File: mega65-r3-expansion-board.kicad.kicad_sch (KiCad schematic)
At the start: 0 parts

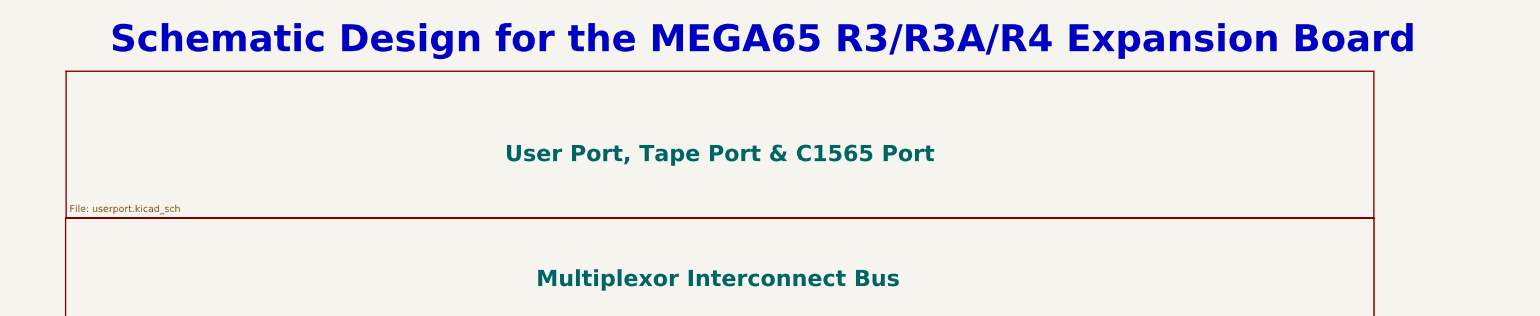
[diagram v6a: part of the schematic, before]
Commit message: begin peeling out C1565 port to separate sheet
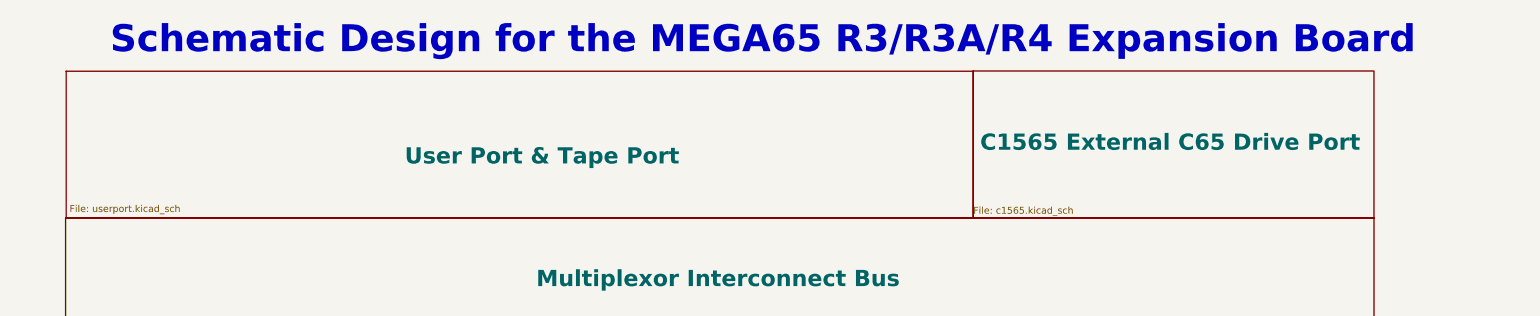
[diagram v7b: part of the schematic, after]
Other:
- sheet User Port, Tape Port & C1565 Port renamed User Port & Tape Port
- added sheet C1565 External C65 Drive Port (c1565.kicad_sch)
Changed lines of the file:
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@@
     (effects (font (size 5 5) (thickness 1) bold) (justify left bottom))
   )
-  (sheet (at 26.1366 63.8175) (size 242.443 27.2415)
+  (sheet (at 26.1366 63.8175) (size 168.1734 27.2415)
     (stroke (width 0.25) (type solid))
     (fill (color 54 142 255 1.0000))
-    (property "Sheetname" "User Port, Tape Port & C1565 Port" (at 107.4928 80.8482 0)
+    (property "Sheetname" "User Port & Tape Port" (at 88.9 81.28 0)
       (effects (font (size 3 3) bold) (justify left bottom))
     )
@@
       )
     )
+  )
+  (sheet (at 194.3072 63.7735) (size 74.2938 27.2606)
+    (stroke (width 0.25) (type solid))
+    (fill (color 0 0 255 1.0000))
+    (property "Sheetname" "C1565 External C65 Drive Port" (at 195.58 78.74 0)
+      (effects (font (size 3 3) bold) (justify left bottom))
+    )
+    (property "Sheetfile" "c1565.kicad_sch" (at 194.31 88.9 0)
+      (effects (font (size 1.27 1.27)) (justify left top))
+    )
+    (instances
+      (project "mega65-r3-expansion-board.kicad"
+        (path "/e63e39d7-6ac0-4ffd-8aa3-1841a4541b55" (page "6"))
+      )
+    )
